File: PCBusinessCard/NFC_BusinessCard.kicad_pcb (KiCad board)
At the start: 2 copper layers, 85.6 x 68.1 mm, 20 parts

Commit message: Support for KiCad 7
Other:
- board text added: "GlennLopez.com"

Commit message: edited contact info
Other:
- board text added: "1-833-445-6739"
- board text added: "glennlopez.com"
- board text added: "me@glennlopez.com"
- board text added: "sms:"
- board text added: "tel:"
- board text removed: "GlennLopez.com"

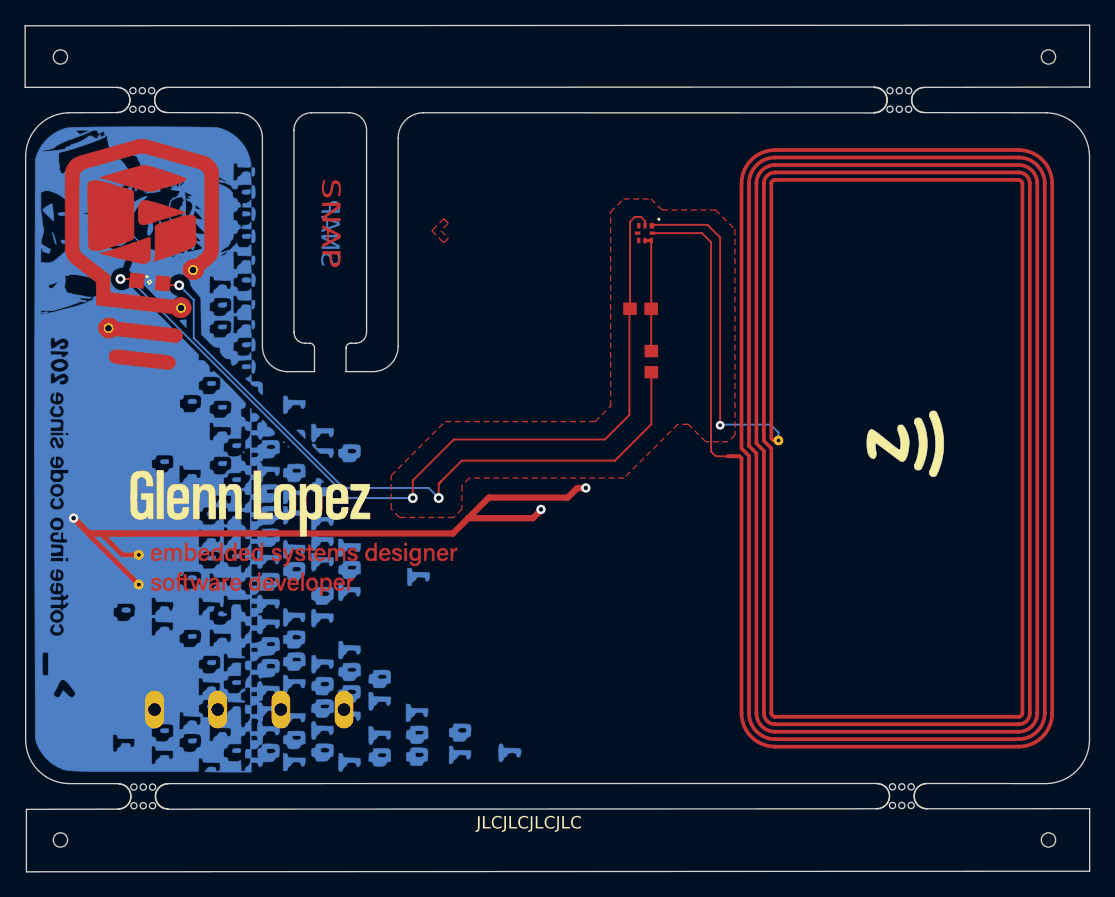
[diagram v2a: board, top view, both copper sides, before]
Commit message: backside redone
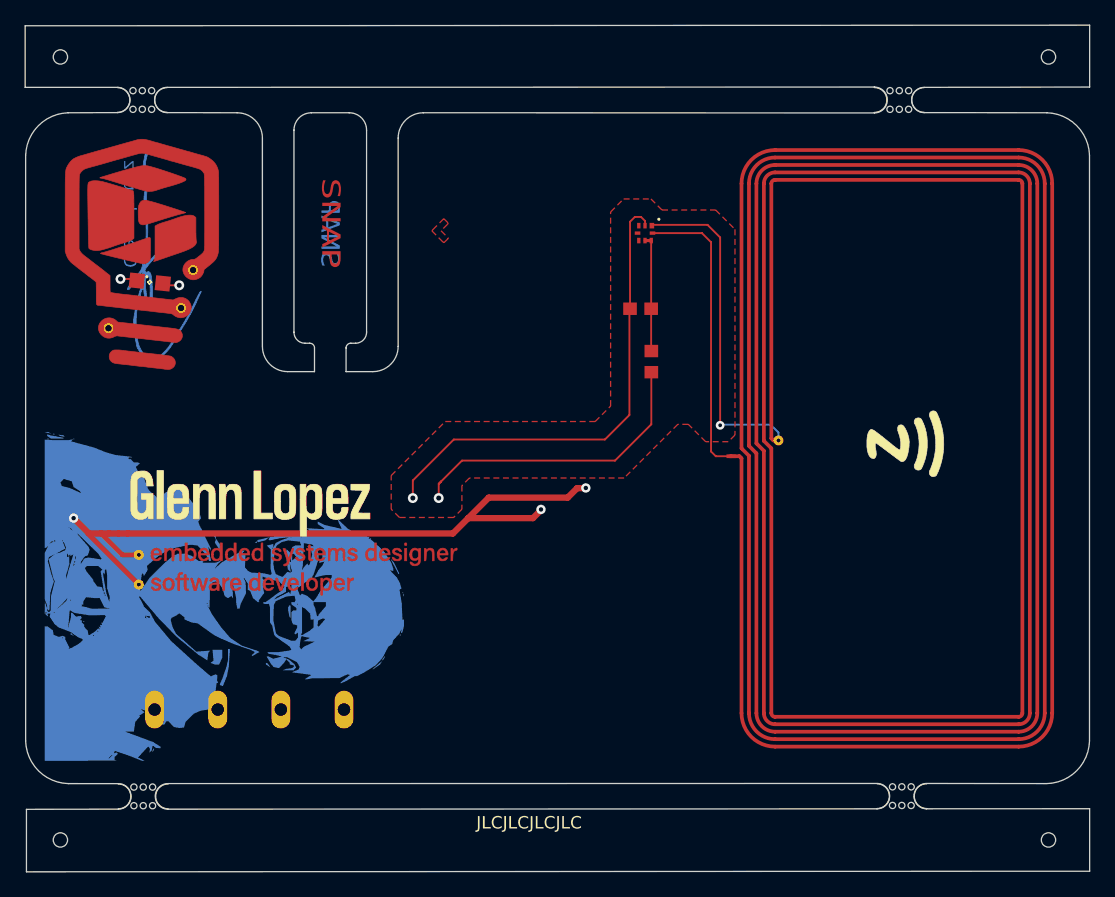
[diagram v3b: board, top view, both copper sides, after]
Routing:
- net N$6: track 70.7 -> 39.8 mm
- net N$4: track 55.8 -> 26.1 mm
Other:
- board text added: "2012"
- board text added: ">_"
- board text added: "coffee into code since"

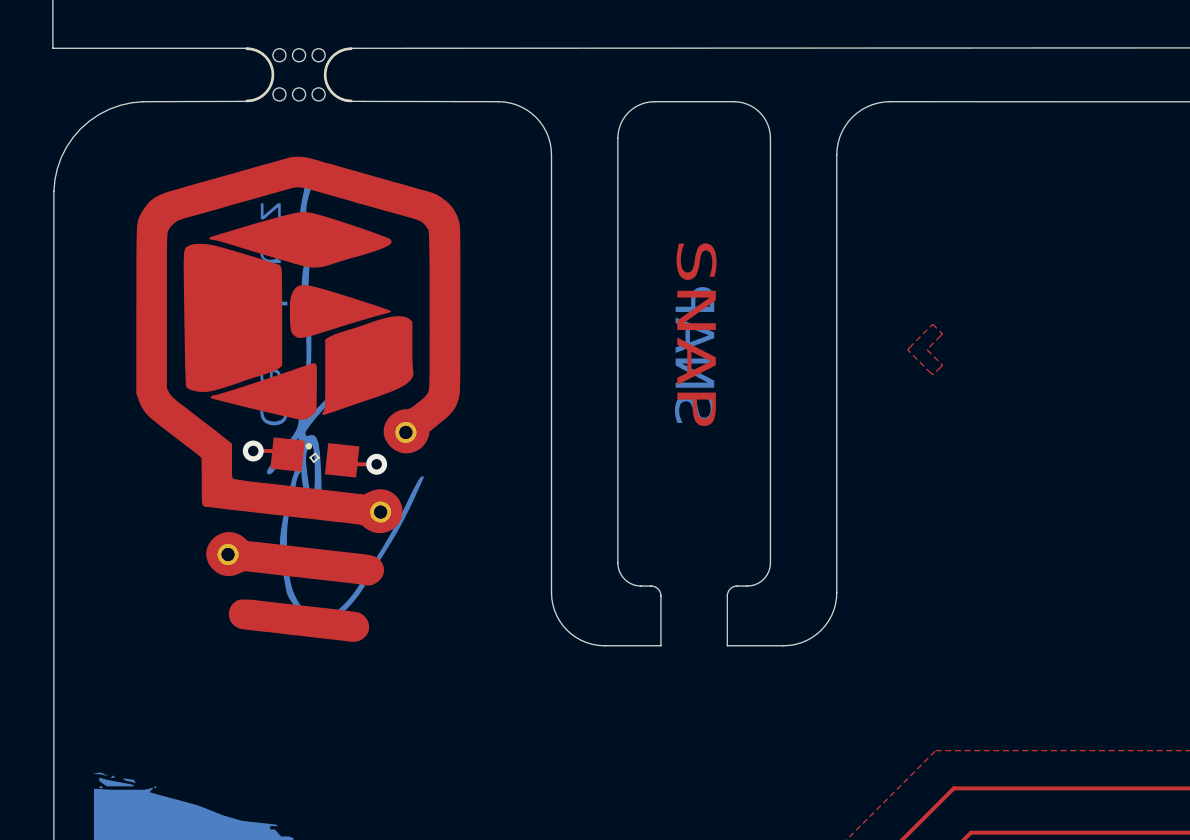
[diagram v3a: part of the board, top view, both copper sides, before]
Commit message: removed placeholder logo
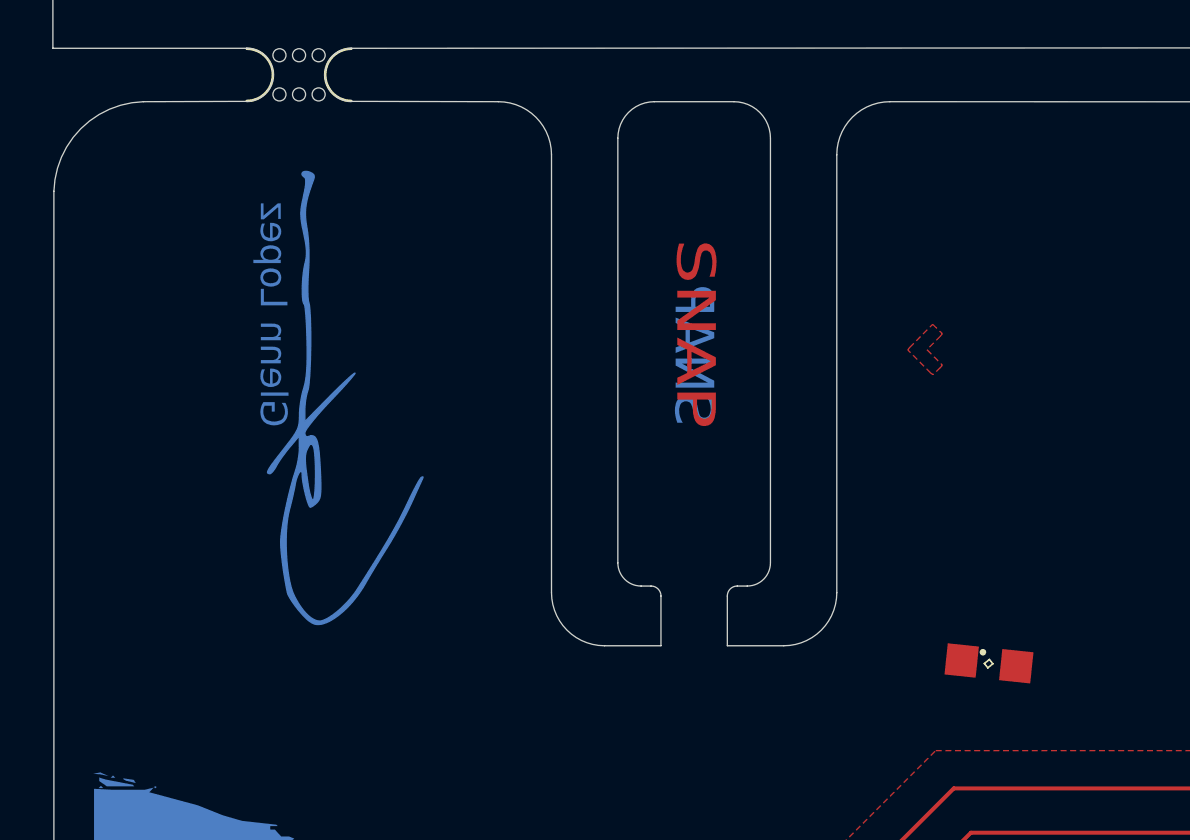
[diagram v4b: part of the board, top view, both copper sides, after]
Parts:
- removed the ? at (80.0, 43.1)
- removed the ? at (79.0, 46.2)
- removed the ? at (73.2, 47.8)
- moved LED1 27.0 mm to (102.3, 52.0)
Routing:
- net N$4: track 26.1 -> 24.7 mm, vias 2 -> 1
- net N$6: track 39.8 -> 38.5 mm, vias 2 -> 1

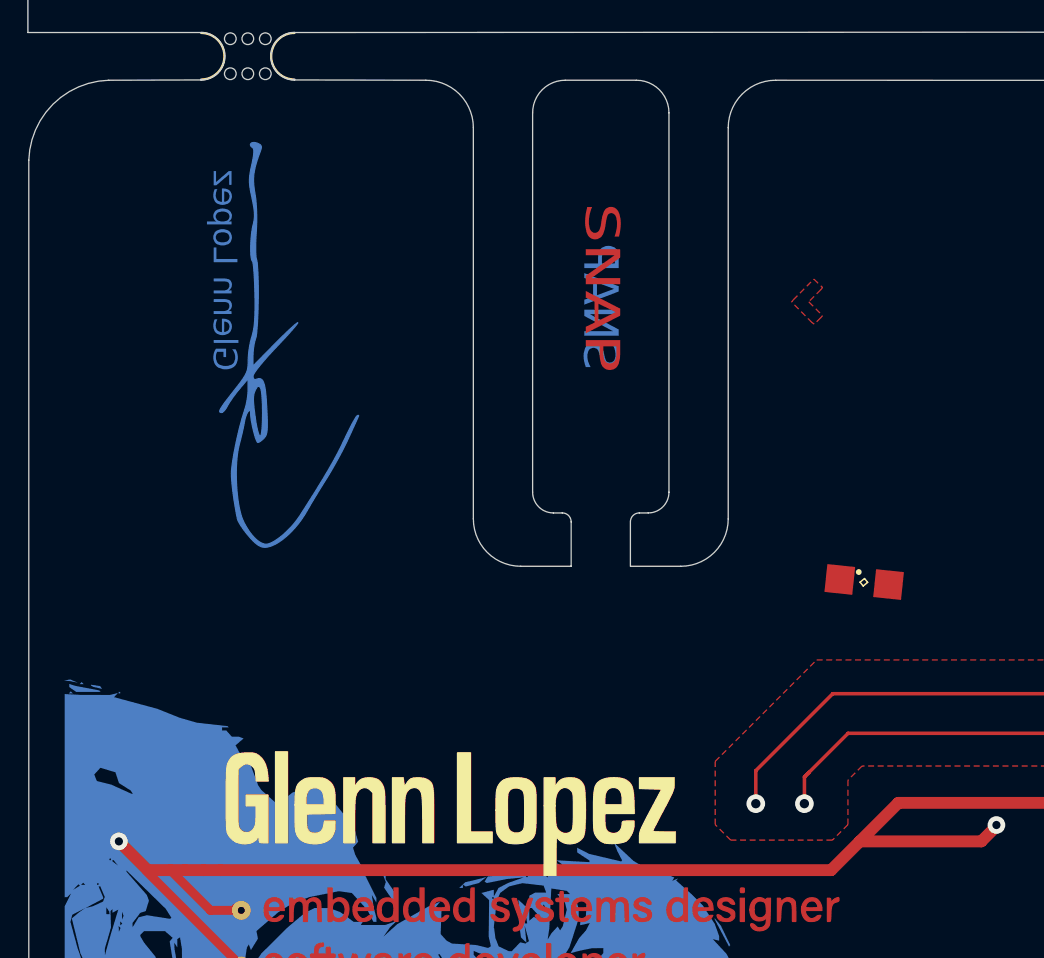
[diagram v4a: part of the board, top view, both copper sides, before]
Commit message: added logo and fixed led
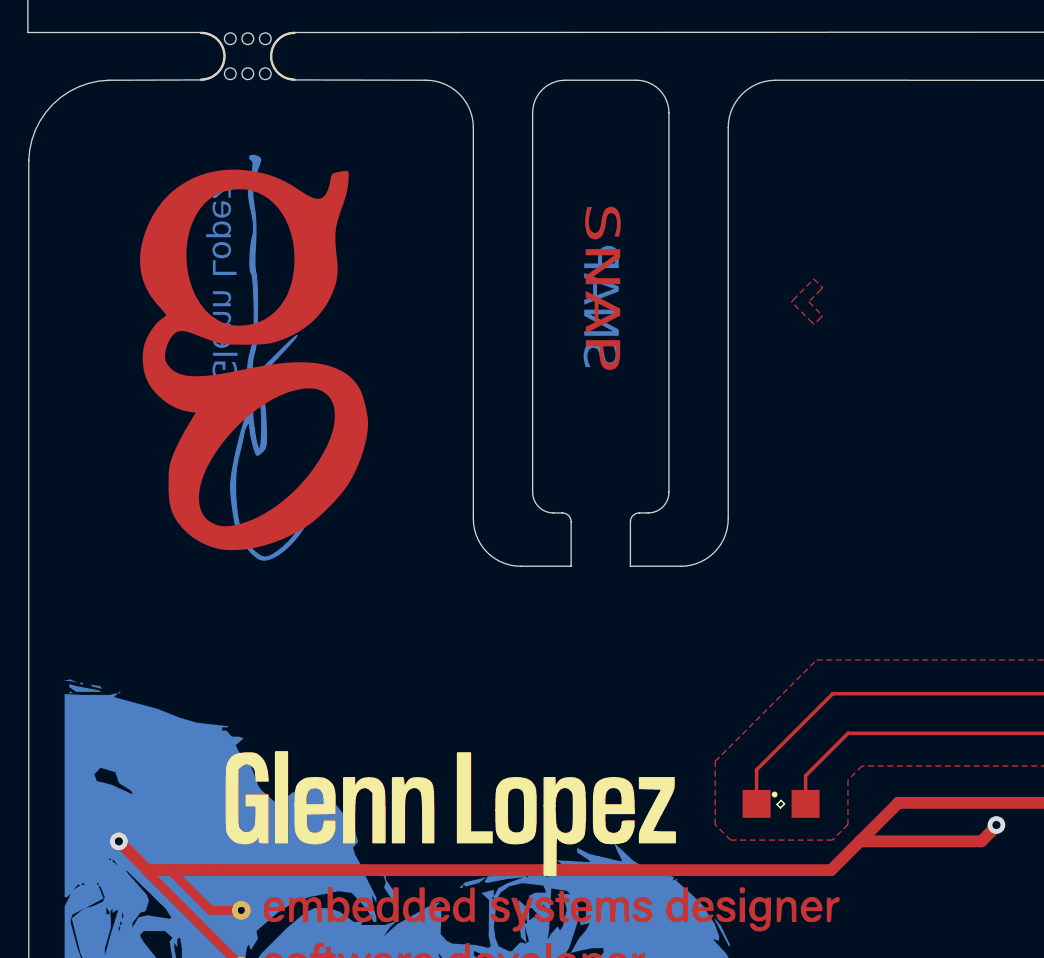
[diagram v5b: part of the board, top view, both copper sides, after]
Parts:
- moved LED1 10.2 mm to (98.8, 61.5), turned to 0 degrees
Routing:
- net N$4: track 24.7 -> 24.4 mm, vias 1 -> 0
- net N$6: vias 1 -> 0
